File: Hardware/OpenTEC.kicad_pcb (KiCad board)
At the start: 4 copper layers, 130 x 90 mm, 72 parts, among them J1 USB_B_Micro, J10 TEMP3, J11 TEC_A, J12 TEC_B, J13 XH2.54, J14 XH2.54, J15 XH2.54, J16 XH2.54, J17 XH2.54, J18 XH2.54, J19 XH2.54, J2 4P Screw Terminal, J20 XH2.54, J21 XH2.54, J22 XH2.54, J23 XH2.54, J24 XH2.54, J25 XH2.54, J26 XH2.54, J27 XH2.54, J28 XH2.54, J3 10P JTAG/SWD, J4 LCD, J5 I2C, J6 BOOT_SEL, J7 TEMP0, J8 TEMP1, J9 TEMP2, U1 AMS1117-5.0, U10 EL357N, U11 STM32F103C8T6, U2 AMS1117-3.3, U3 DMC3021LK4, U4 DMC3021LK4, U5 EL357N, U6 EL357N, U7 DMC3021LK4, U8 DMC3021LK4, U9 EL357N, Y1 16MHz

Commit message: Change H-bridge design
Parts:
- removed the J12 at (200.0, 92.0)
- removed R1, R2, R6, R7: 2K, Resistor_SMD:R_1206_3216Metric
- removed R4, R5, R8, R9: 100, Resistor_SMD:R_0402_1005Metric
- removed U10, U5, U6, U9: EL357N, Package_SO:SOP-4_3.8x4.1mm_P2.54mm
- removed U7, U8: DMC3021LK4, Package_TO_SOT_SMD:TO-252-4
- added C14: 10uF, Capacitor_SMD:C_0805_2012Metric, F.Cu at (185.5, 101.0)
- added C15: 10uF, Capacitor_SMD:C_0805_2012Metric, F.Cu at (185.5, 58.0)
- added C16: 10uF, Capacitor_SMD:C_0805_2012Metric, F.Cu at (139.0, 79.0)
- added C17: 10uF, Capacitor_SMD:C_0805_2012Metric, F.Cu at (139.0, 89.0)
- added C18: 1uF, Capacitor_SMD:C_0805_2012Metric, F.Cu at (147.5, 93.0)
- added C19: 1uF, Capacitor_SMD:C_0805_2012Metric, F.Cu at (147.5, 83.0)
- added D3: B5819W, Diode_SMD:D_SOD-123, F.Cu at (146.0, 89.0)
- added D4: B5819W, Diode_SMD:D_SOD-123, F.Cu at (146.0, 79.0)
- added Q1: FDS6574A, Package_SO:SOIC-8_3.9x4.9mm_P1.27mm, F.Cu at (182.0, 95.0)
- added Q2: FDS6574A, Package_SO:SOIC-8_3.9x4.9mm_P1.27mm, F.Cu at (182.0, 86.0)
- added Q3: FDS6574A, Package_SO:SOIC-8_3.9x4.9mm_P1.27mm, F.Cu at (182.0, 73.0)
- added Q4: FDS6574A, Package_SO:SOIC-8_3.9x4.9mm_P1.27mm, F.Cu at (182.0, 64.0)
- C12, C13: value 5pF -> 30pF
- J11: value TEC_A -> TEC; footprint TerminalBlock:TerminalBlock_bornier-2_P5.08mm -> TerminalBlock:TerminalBlock_bornier-4_P5.08mm
- U3, U4: value DMC3021LK4 -> IR2104; footprint Package_TO_SOT_SMD:TO-252-4 -> Package_SO:SOIC-8_3.9x4.9mm_P1.27mm
- moved U4 51.9 mm to (142.0, 83.0)
- moved U3 51.4 mm to (142.0, 93.0)
- moved J11 20.0 mm to (199.0, 87.0)
- renumbered J28 to J12
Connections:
- J11 pad 1: Net-(J11-Pad1) -> Net-(C18-Pad2)
- J11 pad 2: Net-(J11-Pad2) -> Net-(C18-Pad2)
- U11 pad 40: HB_A1 -> HB1
- U11 pad 41: HB_A2 -> HB1_SD
- U11 pad 42: HB_B1 -> HB2
- U11 pad 43: HB_B2 -> HB2_SD
- U3 pad 1: GND -> +3V3
- U3 pad 2: Net-(R1-Pad2) -> HB1
- U3 pad 3: Net-(J11-Pad1) -> HB1_SD
- U3 pad 4: +12V -> GND
- U3 pad 5: Net-(R1-Pad2) -> Net-(Q2-Pad4)
- U4 pad 1: GND -> +3V3
- U4 pad 2: Net-(R2-Pad2) -> HB2
- U4 pad 3: Net-(J11-Pad2) -> HB2_SD
- U4 pad 4: +12V -> GND
- U4 pad 5: Net-(R2-Pad2) -> Net-(Q4-Pad4)
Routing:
- net Net-(R2-Pad2): track 61.7 -> 0.00 mm
- net Net-(Q4-Pad4): track 0.00 -> 55.0 mm
- net Net-(R1-Pad2): track 53.2 -> 0.00 mm
- net Net-(Q3-Pad4): track 0.00 -> 52.2 mm
- net Net-(C19-Pad2): track 0.00 -> 51.4 mm, vias 0 -> 2
- net Net-(R7-Pad2): track 49.3 -> 0.00 mm
- net Net-(R6-Pad2): track 47.2 -> 0.00 mm
- net HB_A2: track 44.0 -> 0.00 mm, vias 2 -> 0
- net HB2_SD: track 0.00 -> 43.0 mm, vias 0 -> 2
- net Net-(Q1-Pad4): track 0.00 -> 42.6 mm
- net HB_B1: track 42.1 -> 0.00 mm, vias 2 -> 0
- net Net-(Q2-Pad4): track 0.00 -> 41.2 mm, vias 0 -> 2
- net HB_A1: track 41.0 -> 0.00 mm, vias 2 -> 0
- net HB2: track 0.00 -> 40.1 mm, vias 0 -> 2
- net HB_B2: track 39.0 -> 0.00 mm, vias 2 -> 0
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- added copper zone on B.Cu, net +12V
- added copper zone on B.Cu, net GND
- added copper zone on F.Cu, net Net-(C18-Pad2)
- added copper zone on F.Cu, net Net-(C19-Pad2)
- removed copper zone on F.Cu, net Net-(J11-Pad1)
- removed copper zone on F.Cu, net Net-(J11-Pad2)
- removed copper zone on F.Cu, net Net-(J12-Pad1)
- removed copper zone on F.Cu, net Net-(J12-Pad2)

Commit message: Fix USB Micro B connector footprint
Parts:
- J1: footprint Connector_USB:USB_Micro-B_GCT_USB3076-30-A -> Connector_USB:USB_Micro-B_Amphenol_10103594-0001LF_Horizontal
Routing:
- net +5V: track 77.9 -> 85.1 mm
- net USB_D+: track 50.0 -> 49.1 mm

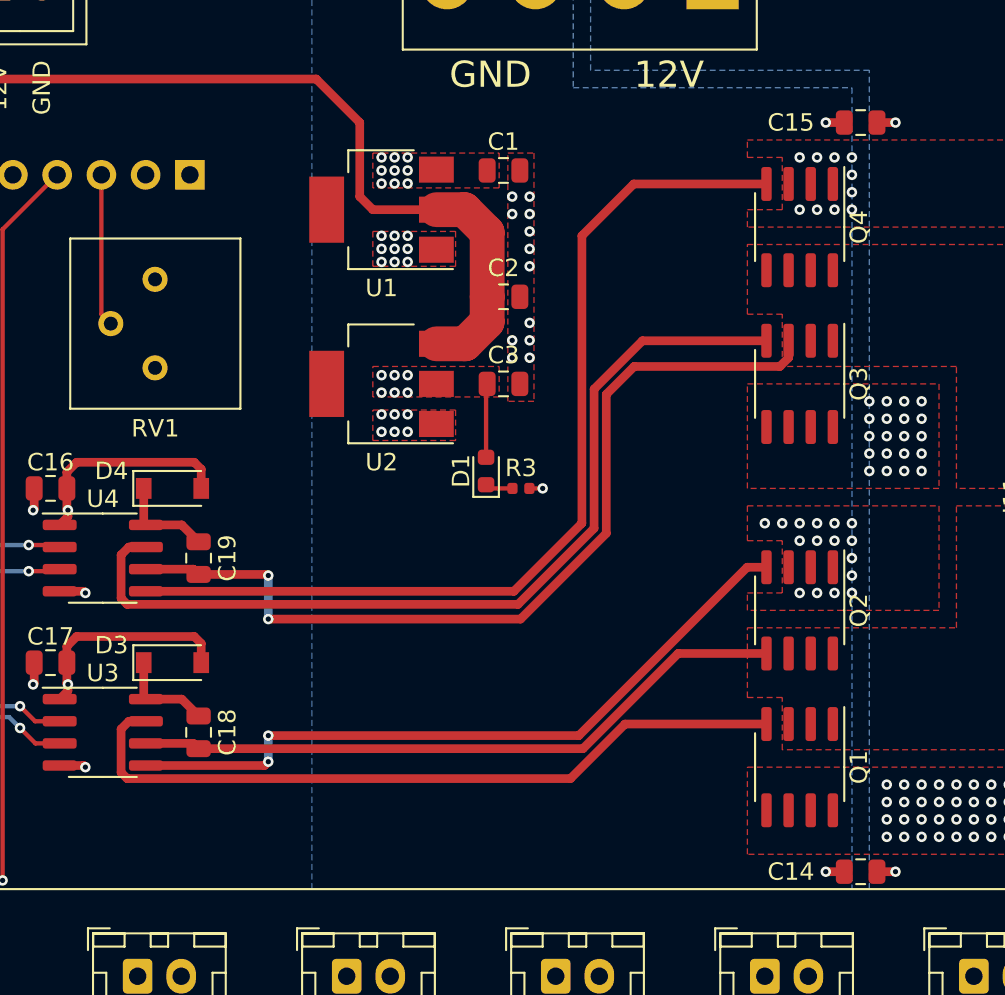
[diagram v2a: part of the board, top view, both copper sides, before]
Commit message: Add BFC to H-bridge
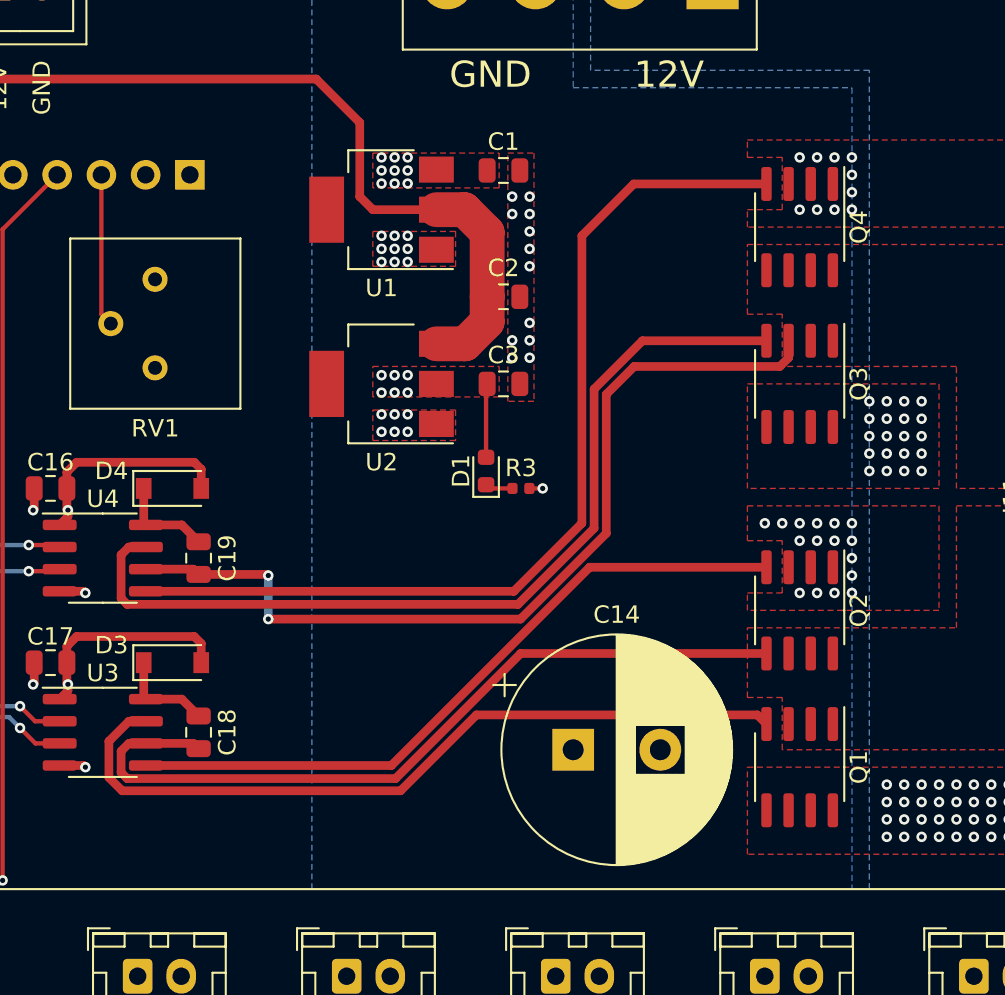
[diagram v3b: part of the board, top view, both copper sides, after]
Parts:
- removed C15: 10uF, Capacitor_SMD:C_0805_2012Metric
- C14: value 10uF -> 1000uF; footprint Capacitor_SMD:C_0805_2012Metric -> Capacitor_THT:CP_Radial_D13.0mm_P5.00mm
- moved C14 17.9 mm to (169.0, 94.0), turned to 0 degrees
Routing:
- net Net-(C18-Pad2): track 38.0 -> 46.1 mm
- net Net-(Q1-Pad4): track 42.6 -> 44.8 mm
- net GND: track 32.4 -> 30.3 mm, vias 87 -> 85
- net +12V: track 67.6 -> 65.5 mm, vias 71 -> 69
- net Net-(Q2-Pad4): track 41.2 -> 40.3 mm, vias 2 -> 0

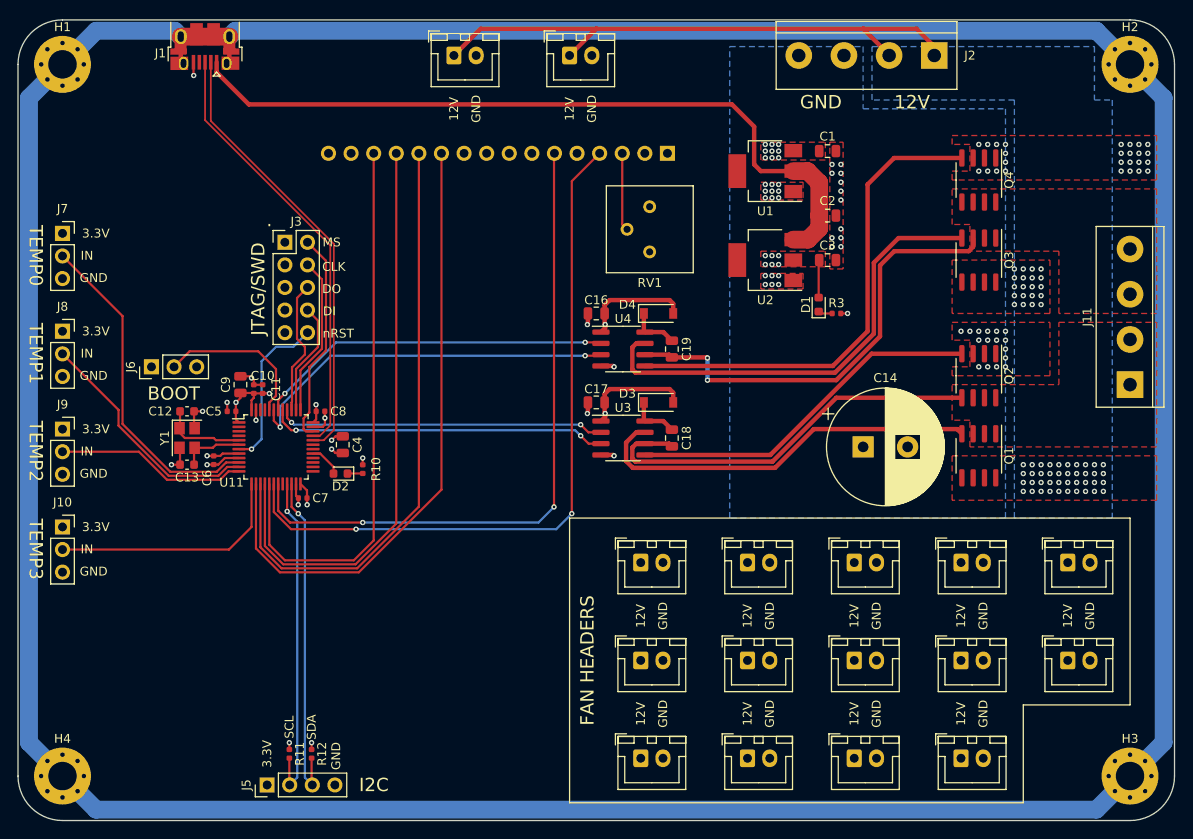
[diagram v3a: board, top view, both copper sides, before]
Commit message: Remove unused USB port and 5V LDO
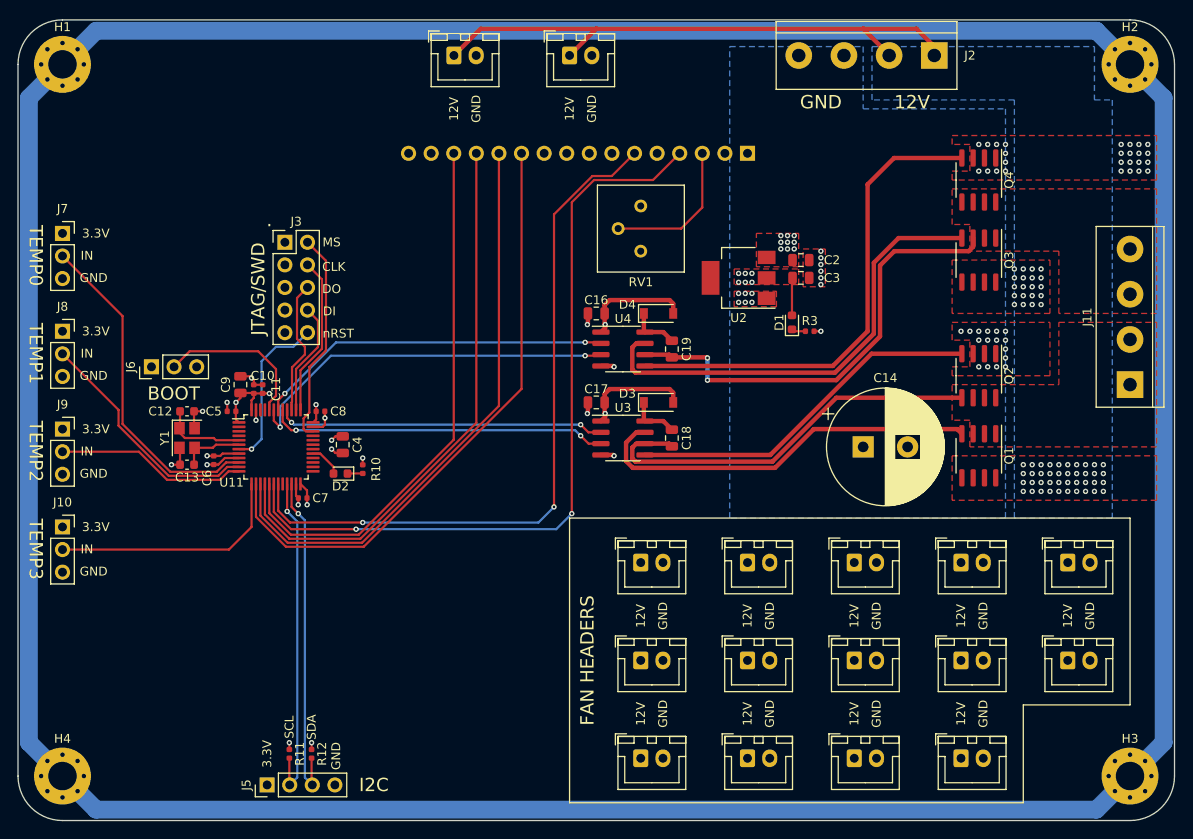
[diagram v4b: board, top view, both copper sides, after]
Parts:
- removed C1: 10uF, Capacitor_SMD:C_0805_2012Metric
- removed J1: USB_B_Micro, Connector_USB:USB_Micro-B_Amphenol_10103594-0001LF_Horizontal
- removed U1: AMS1117-5.0, Package_TO_SOT_SMD:SOT-223-3_TabPin2
- moved J4 9.00 mm to (156.0, 61.0)
- moved C2 5.83 mm to (162.0, 73.0)
- moved C3 3.61 mm to (162.0, 75.0)
- moved D1 3.61 mm to (161.0, 80.0)
- moved R3 3.61 mm to (163.0, 81.0)
- moved U2 3.61 mm to (155.0, 75.0)
- moved RV1 1.00 mm to (144.0, 66.9)
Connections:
- C2 pad 1: +5V -> +12V
- U11 pad 32: USB_D- -> Net-(U11-Pad32)
- U11 pad 33: USB_D+ -> Net-(U11-Pad33)
- U2 pad 3: +5V -> +12V
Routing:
- net +5V: track 85.1 -> 0.00 mm
- net USB_D-: track 49.9 -> 0.00 mm
- net USB_D+: track 49.1 -> 0.00 mm
- net Net-(J4-Pad3): track 8.76 -> 16.5 mm
- net LCD_RS: track 80.0 -> 87.6 mm
- net Earth: track 419.3 -> 412.5 mm
- net LCD_EN: track 75.1 -> 80.1 mm
- net LCD_D5: track 68.5 -> 66.4 mm
- net LCD_D7: track 63.7 -> 61.6 mm
- net LCD_D6: track 66.1 -> 64.0 mm
- net LCD_D4: track 70.9 -> 68.8 mm
- net GND: track 30.3 -> 28.8 mm, vias 85 -> 69

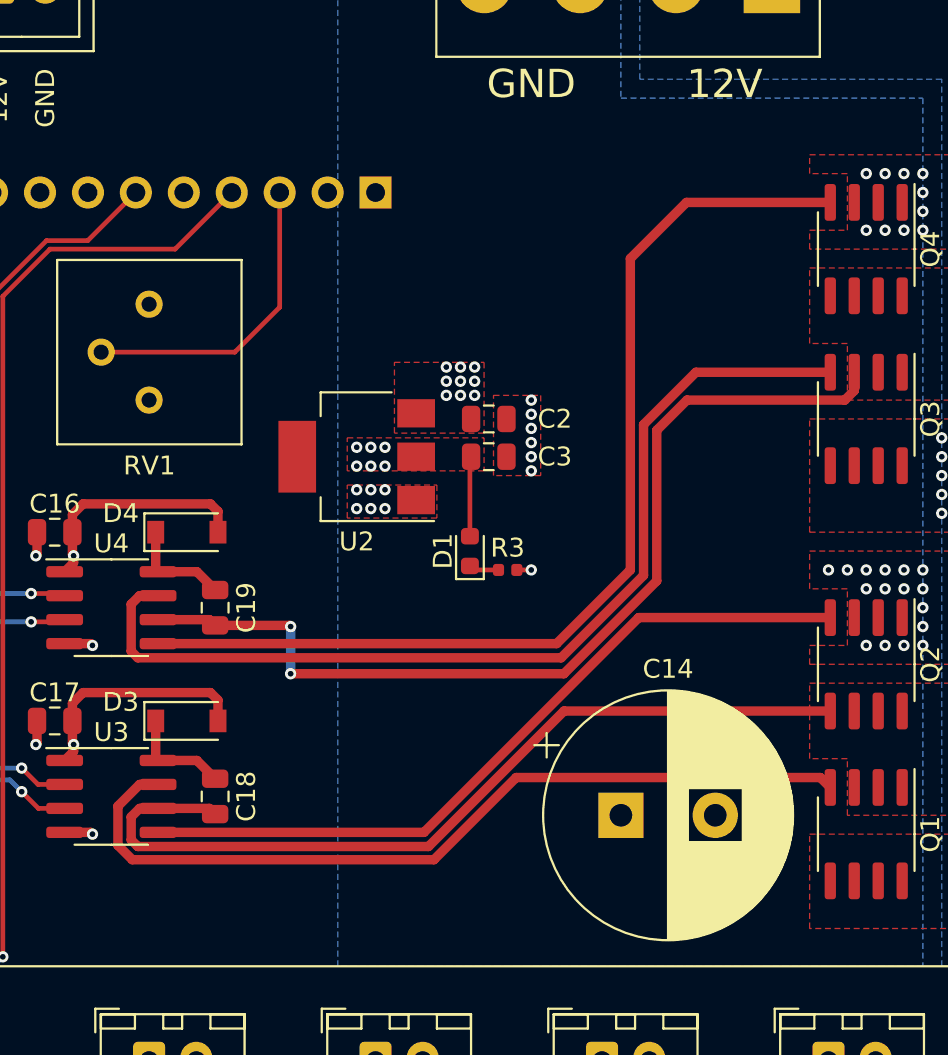
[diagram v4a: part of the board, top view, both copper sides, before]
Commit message: Add RC filter to 3.3V LDO input
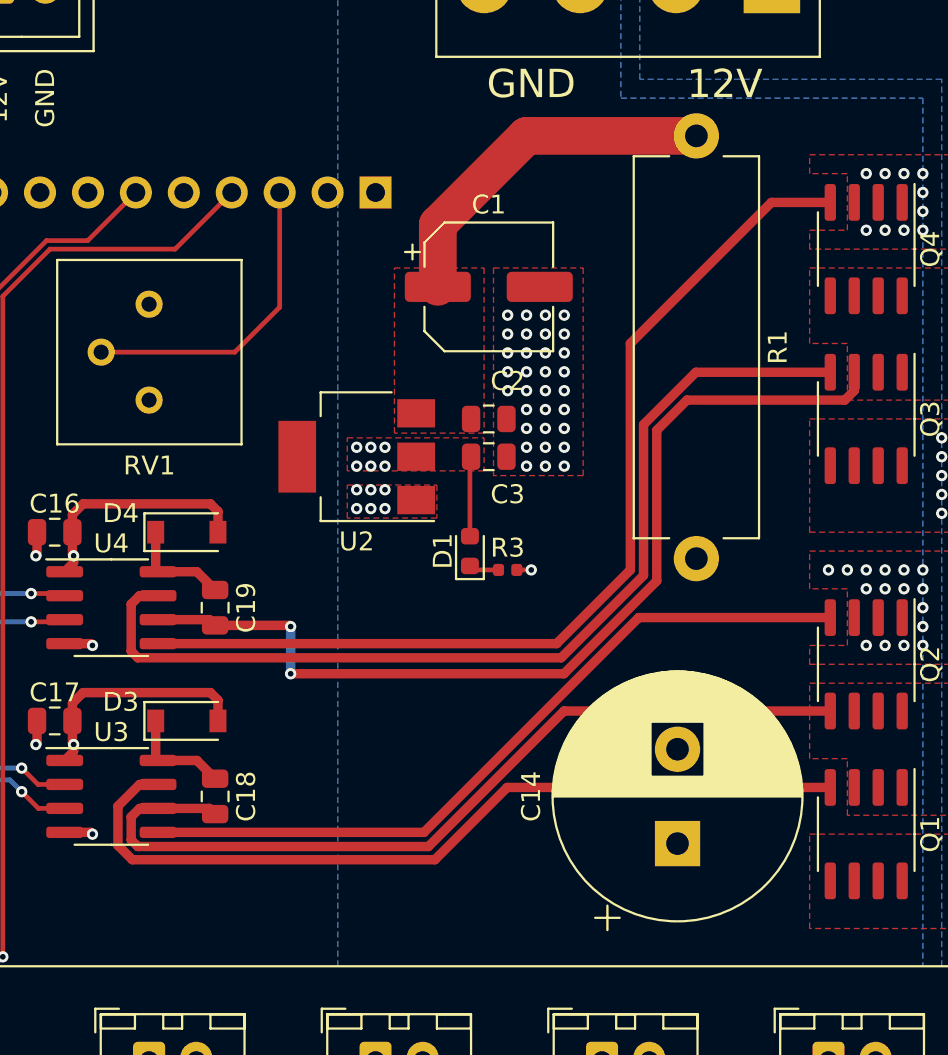
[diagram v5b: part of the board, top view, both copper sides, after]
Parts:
- added C1: 100uF, Capacitor_SMD:CP_Elec_6.3x5.8, F.Cu at (162.0, 66.0)
- added R1: 10, Resistor_THT:R_Axial_Power_L20.0mm_W6.4mm_P22.40mm, F.Cu at (173.0, 58.0)
- moved C14 3.35 mm to (172.0, 95.5), turned to 90 degrees
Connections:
- C2 pad 1: +12V -> Net-(C1-Pad1)
- U2 pad 3: +12V -> Net-(C1-Pad1)
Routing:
- net Net-(C1-Pad1): track 0.00 -> 18.9 mm
- net Net-(Q4-Pad4): track 55.0 -> 52.3 mm
- net GND: vias 69 -> 95
- net +12V: vias 69 -> 60
- added copper zone on F.Cu, net Net-(C1-Pad1)
